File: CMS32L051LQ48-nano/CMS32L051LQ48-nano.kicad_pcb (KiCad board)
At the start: 4 copper layers, 18 x 43.2 mm, 26 parts, among them J101 Board Pin, J102 Board Pin, J103 USB_B_Micro, J105 Connection to DAPLink Board, U201 CMS32L051LQ48, U301 AP2127K-ADJ

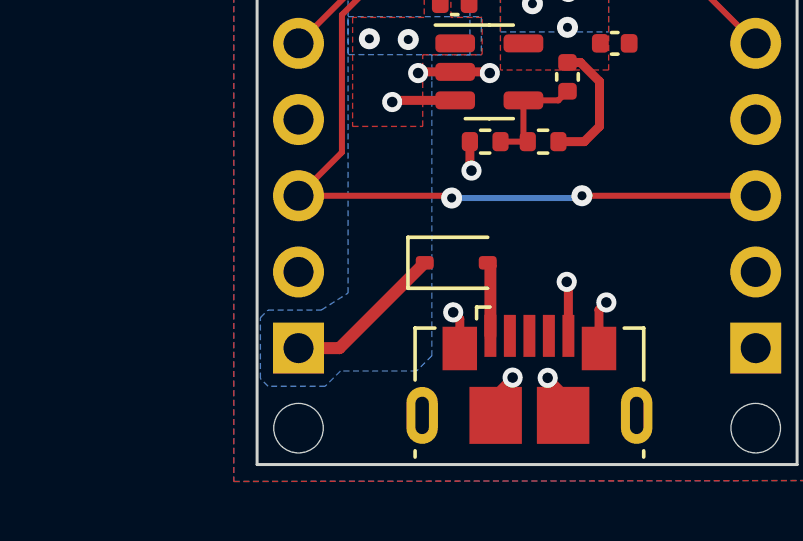
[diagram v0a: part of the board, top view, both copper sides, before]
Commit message: L051: added Vin zone
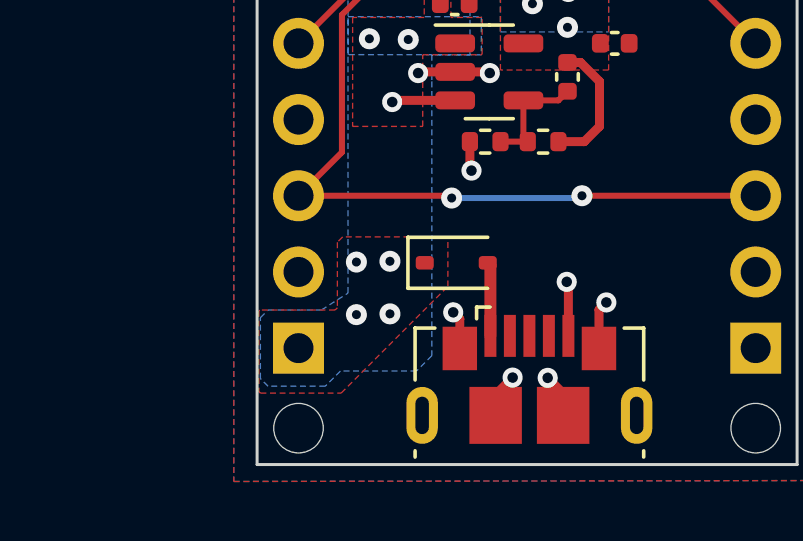
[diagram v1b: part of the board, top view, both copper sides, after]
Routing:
- net /V_{IN}: track 7.51 -> 2.12 mm, vias 3 -> 7
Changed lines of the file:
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@@
   (via (at 99.5934 72.1868) (size 0.67) (drill 0.35) (layers "F.Cu" "B.Cu") (net 2))
   (via (at 100.6348 85.8012) (size 0.67) (drill 0.35) (layers "F.Cu" "B.Cu") (net 2))
-  (segment (start 93.057 88.011) (end 91.694 88.011) (width 0.4) (layer "F.Cu") (net 3))
   (segment (start 94.873 79.752) (end 94.8182 79.8068) (width 0.3) (layer "F.Cu") (net 3))
   (segment (start 96.916 79.752) (end 94.873 79.752) (width 0.3) (layer "F.Cu") (net 3))
-  (segment (start 95.9018 85.1662) (end 93.057 88.011) (width 0.4) (layer "F.Cu") (net 3))
   (via (at 94.0562 77.6986) (size 0.7) (drill 0.3) (layers "F.Cu" "B.Cu") (free) (net 3))
+  (via (at 94.742 86.868) (size 0.7) (drill 0.3) (layers "F.Cu" "B.Cu") (free) (net 3))
+  (via (at 93.6244 85.1408) (size 0.7) (drill 0.3) (layers "F.Cu" "B.Cu") (free) (net 3))
+  (via (at 93.6244 86.8934) (size 0.7) (drill 0.3) (layers "F.Cu" "B.Cu") (free) (net 3))
   (via (at 94.8182 79.8068) (size 0.67) (drill 0.35) (layers "F.Cu" "B.Cu") (net 3))
   (via (at 95.3516 77.724) (size 0.7) (drill 0.3) (layers "F.Cu" "B.Cu") (free) (net 3))
+  (via (at 94.742 85.1154) (size 0.7) (drill 0.3) (layers "F.Cu" "B.Cu") (free) (net 3))
   (segment (start 99.191 79.752) (end 99.191 80.9812) (width 0.2) (layer "F.Cu") (net 4))
   (segment (start 99.191 80.9812) (end 99.3374 81.1276) (width 0.2) (layer "F.Cu") (net 4))
@@
   (segment (start 95.885 56.880929) (end 95.885 50.3428) (width 0.2) (layer "F.Cu") (net 59))
   (segment (start 97.0386 58.034529) (end 95.885 56.880929) (width 0.2) (layer "F.Cu") (net 59))
+  (zone (net 3) (net_name "/V_{IN}") (layer "F.Cu") (name "V_in") (hatch edge 0.5)
+    (priority 25)
+    (connect_pads yes (clearance 0.15))
+    (min_thickness 0.1) (filled_areas_thickness no)
+    (fill yes (thermal_gap 0.1) (thermal_bridge_width 0.2))
+    (polygon
+      (pts
+        (xy 96.6724 84.3026)
+        (xy 93.1672 84.3026)
+        (xy 92.9894 84.4804)
+        (xy 92.9894 86.6648)
+        (xy 92.9132 86.741)
+        (xy 90.3986 86.741)
+        (xy 90.3732 86.7664)
+        (xy 90.3732 89.4588)
+        (xy 90.424 89.5096)
+        (xy 93.1164 89.5096)
+        (xy 96.6724 85.9536)
+      )
+    )
+  )
   (zone (net 5) (net_name "/Regulator_V_{OUT}") (layer "F.Cu") (name "RegV_{OUT}") (hatch edge 0.5)
     (priority 20)

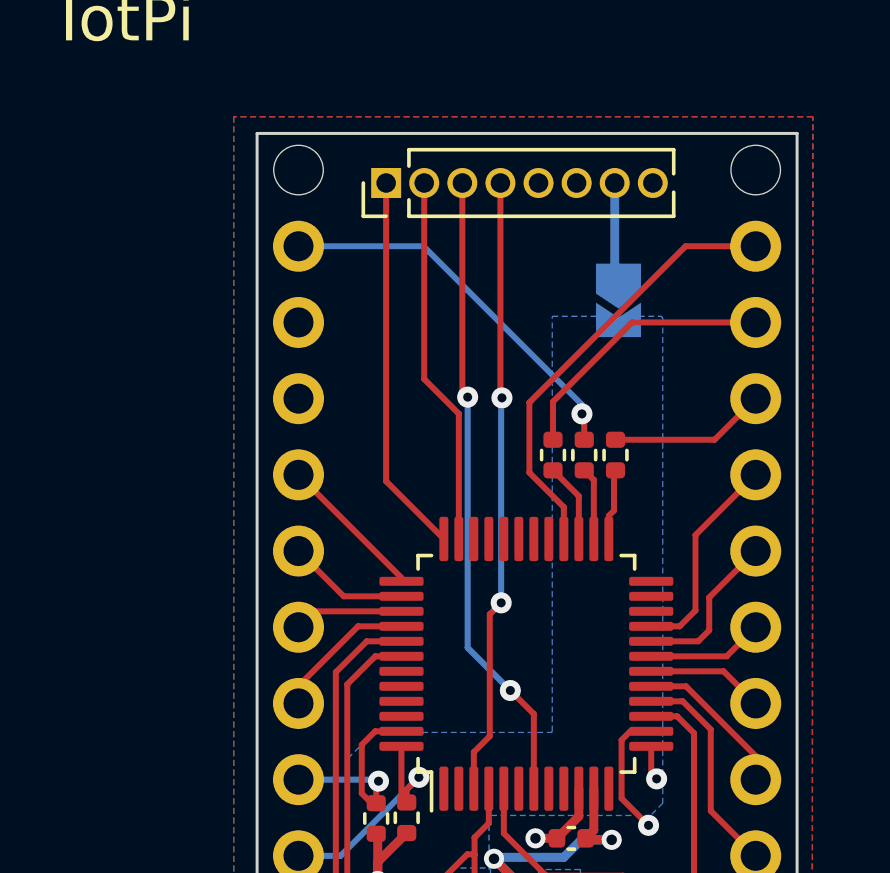
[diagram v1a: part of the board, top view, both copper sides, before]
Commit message: L051: make space for LEDs
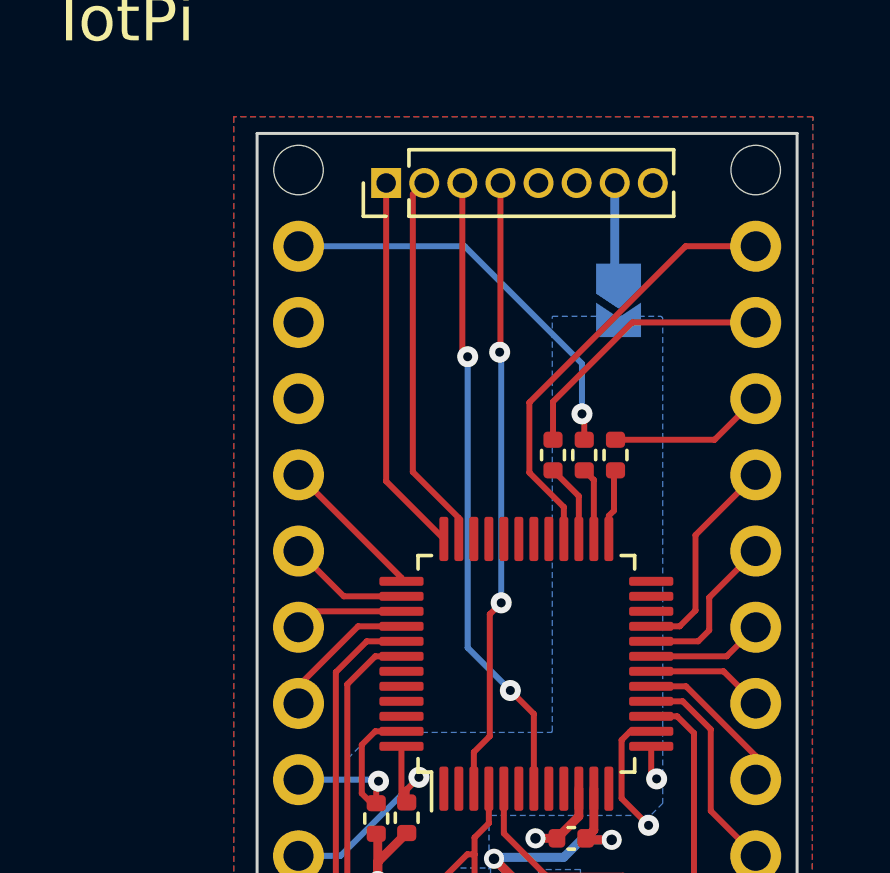
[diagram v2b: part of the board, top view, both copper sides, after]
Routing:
- net /MCU/D13/SCK: track 12.8 -> 13.6 mm
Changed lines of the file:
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@@
   (via (at 99.4918 76.5302) (size 0.7) (drill 0.3) (layers "F.Cu" "B.Cu") (free) (net 5))
   (via (at 100.6602 77.3176) (size 0.7) (drill 0.3) (layers "F.Cu" "B.Cu") (free) (net 5))
-  (segment (start 97.155 57.3024) (end 97.155 50.3428) (width 0.2) (layer "F.Cu") (net 6))
+  (segment (start 97.3328 56.134) (end 97.155 55.9562) (width 0.2) (layer "F.Cu") (net 6))
+  (segment (start 97.155 55.9562) (end 97.155 50.3428) (width 0.2) (layer "F.Cu") (net 6))
   (segment (start 98.7552 67.2592) (end 99.5386 68.0426) (width 0.2) (layer "F.Cu") (net 6))
-  (segment (start 97.3328 57.4802) (end 97.155 57.3024) (width 0.2) (layer "F.Cu") (net 6))
   (segment (start 99.5386 68.0426) (end 99.5386 70.5327) (width 0.2) (layer "F.Cu") (net 6))
-  (via (at 97.3328 57.4802) (size 0.7) (drill 0.3) (layers "F.Cu" "B.Cu") (net 6))
+  (via (at 97.3328 56.134) (size 0.7) (drill 0.3) (layers "F.Cu" "B.Cu") (net 6))
   (via (at 98.7552 67.2592) (size 0.7) (drill 0.3) (layers "F.Cu" "B.Cu") (net 6))
-  (segment (start 97.3328 65.8368) (end 97.3328 57.4802) (width 0.2) (layer "B.Cu") (net 6))
-  (segment (start 98.7552 67.2592) (end 97.3328 65.8368) (width 0.2) (layer "B.Cu") (net 6))
+  (segment (start 97.3328 56.134) (end 97.3328 65.8368) (width 0.2) (layer "B.Cu") (net 6))
+  (segment (start 97.3328 65.8368) (end 98.7552 67.2592) (width 0.2) (layer "B.Cu") (net 6))
+  (segment (start 98.425 55.9562) (end 98.425 50.3428) (width 0.2) (layer "F.Cu") (net 7))
   (segment (start 97.5386 70.5327) (end 97.5386 69.314) (width 0.2) (layer "F.Cu") (net 7))
   (segment (start 97.5386 69.314) (end 98.0694 68.7832) (width 0.2) (layer "F.Cu") (net 7))
   (segment (start 98.0694 64.7192) (end 98.4504 64.3382) (width 0.2) (layer "F.Cu") (net 7))
-  (segment (start 98.4758 57.5056) (end 98.425 57.4548) (width 0.2) (layer "F.Cu") (net 7))
   (segment (start 98.0694 68.7832) (end 98.0694 64.7192) (width 0.2) (layer "F.Cu") (net 7))
-  (segment (start 98.425 57.4548) (end 98.425 50.3428) (width 0.2) (layer "F.Cu") (net 7))
+  (segment (start 98.3996 55.9816) (end 98.425 55.9562) (width 0.2) (layer "F.Cu") (net 7))
   (via (at 98.4504 64.3382) (size 0.7) (drill 0.3) (layers "F.Cu" "B.Cu") (net 7))
-  (via (at 98.4758 57.5056) (size 0.7) (drill 0.3) (layers "F.Cu" "B.Cu") (net 7))
-  (segment (start 98.4504 57.531) (end 98.4758 57.5056) (width 0.2) (layer "B.Cu") (net 7))
-  (segment (start 98.4504 64.3382) (end 98.4504 57.531) (width 0.2) (layer "B.Cu") (net 7))
+  (via (at 98.3996 55.9816) (size 0.7) (drill 0.3) (layers "F.Cu" "B.Cu") (net 7))
+  (segment (start 98.4504 56.0324) (end 98.4504 64.3382) (width 0.2) (layer "B.Cu") (net 7))
+  (segment (start 98.3996 55.9816) (end 98.4504 56.0324) (width 0.2) (layer "B.Cu") (net 7))
   (segment (start 97.6604 75.1586) (end 97.6604 74.1686) (width 0.2) (layer "F.Cu") (net 15))
   (segment (start 98.0386 71.6842) (end 98.0386 70.5327) (width 0.2) (layer "F.Cu") (net 15))
@@
   (segment (start 101.219 58.9006) (end 101.219 58.1152) (width 0.2) (layer "F.Cu") (net 37))
   (via (at 101.1428 58.039) (size 0.7) (drill 0.3) (layers "F.Cu" "B.Cu") (net 37))
-  (segment (start 101.1428 58.039) (end 101.1428 57.7342) (width 0.2) (layer "B.Cu") (net 37))
-  (segment (start 95.8596 52.451) (end 91.694 52.451) (width 0.2) (layer "B.Cu") (net 37))
-  (segment (start 101.1428 57.7342) (end 95.8596 52.451) (width 0.2) (layer "B.Cu") (net 37))
+  (segment (start 101.1428 58.039) (end 101.1428 56.3626) (width 0.2) (layer "B.Cu") (net 37))
+  (segment (start 97.2312 52.451) (end 91.694 52.451) (width 0.2) (layer "B.Cu") (net 37))
+  (segment (start 101.1428 56.3626) (end 97.2312 52.451) (width 0.2) (layer "B.Cu") (net 37))
   (segment (start 101.5386 62.2077) (end 101.5386 60.2402) (width 0.2) (layer "F.Cu") (net 38))
   (segment (start 101.5386 60.2402) (end 101.219 59.9206) (width 0.2) (layer "F.Cu") (net 38))
@@
   (segment (start 96.5386 62.2077) (end 94.615 60.2841) (width 0.2) (layer "F.Cu") (net 58))
   (segment (start 94.615 60.2841) (end 94.615 50.3428) (width 0.2) (layer "F.Cu") (net 58))
-  (segment (start 97.0386 62.2077) (end 97.0386 58.034529) (width 0.2) (layer "F.Cu") (net 59))
-  (segment (start 95.885 56.880929) (end 95.885 50.3428) (width 0.2) (layer "F.Cu") (net 59))
-  (segment (start 97.0386 58.034529) (end 95.885 56.880929) (width 0.2) (layer "F.Cu") (net 59))
+  (segment (start 95.504 59.975981) (end 95.504 50.7238) (width 0.2) (layer "F.Cu") (net 59))
+  (segment (start 97.0386 62.2077) (end 97.0386 61.510581) (width 0.2) (layer "F.Cu") (net 59))
+  (segment (start 97.0386 61.510581) (end 95.504 59.975981) (width 0.2) (layer "F.Cu") (net 59))
+  (segment (start 95.504 50.7238) (end 95.885 50.3428) (width 0.2) (layer "F.Cu") (net 59))
   (zone (net 3) (net_name "/V_{IN}") (layer "F.Cu") (name "V_in") (hatch edge 0.5)
     (priority 25)

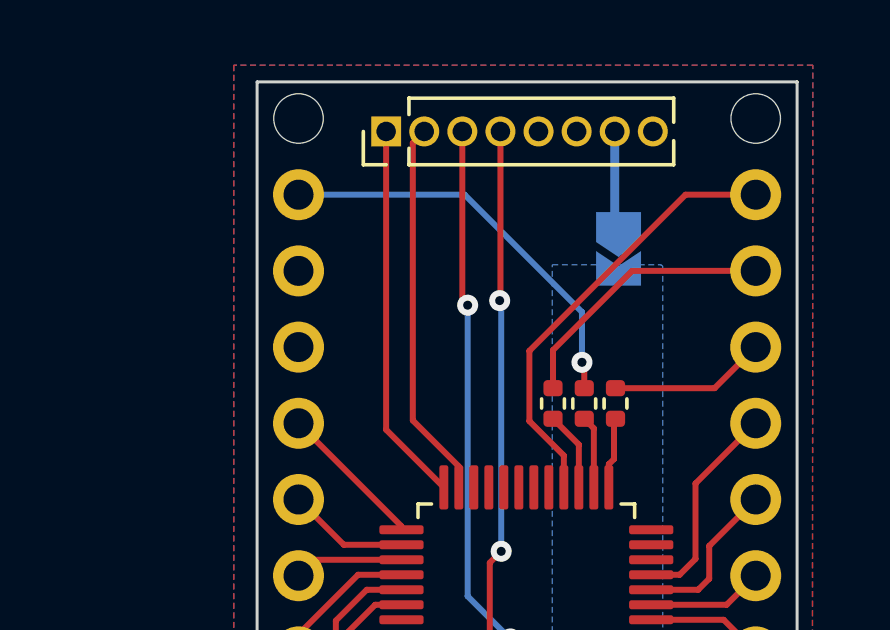
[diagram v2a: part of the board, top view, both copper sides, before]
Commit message: added two LEDs
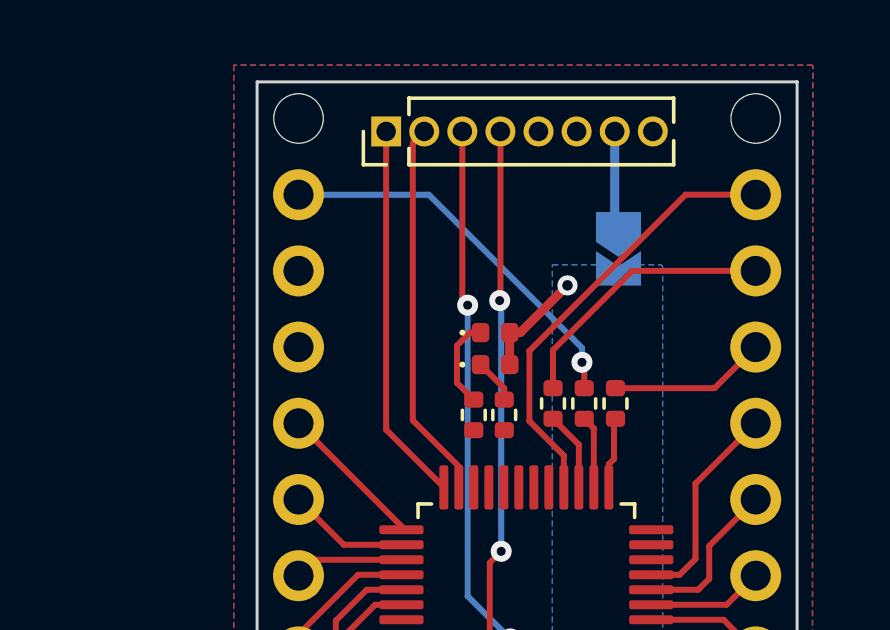
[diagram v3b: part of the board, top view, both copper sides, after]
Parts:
- added D201: LED, LED_SMD:LED_0402_1005Metric, F.Cu at (98.2, 57.0)
- added D202: LED, LED_SMD:LED_0402_1005Metric, F.Cu at (98.2, 58.1)
- added R207: 200R, Resistor_SMD:R_0402_1005Metric, F.Cu at (97.5, 59.8)
- added R208: 200R, Resistor_SMD:R_0402_1005Metric, F.Cu at (98.6, 59.8)
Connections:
- U201 pad 33: unconnected-(U201-P11-Pad33) -> /MCU/LED2
- U201 pad 34: unconnected-(U201-P10-Pad34) -> /MCU/LED1
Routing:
- net /V_{IN}: track 2.12 -> 5.77 mm, vias 7 -> 8
- net Net-(D201-K): track 0.00 -> 3.00 mm
- net Net-(D202-K): track 0.00 -> 1.49 mm
- net /MCU/D13/SCK: track 13.6 -> 12.9 mm

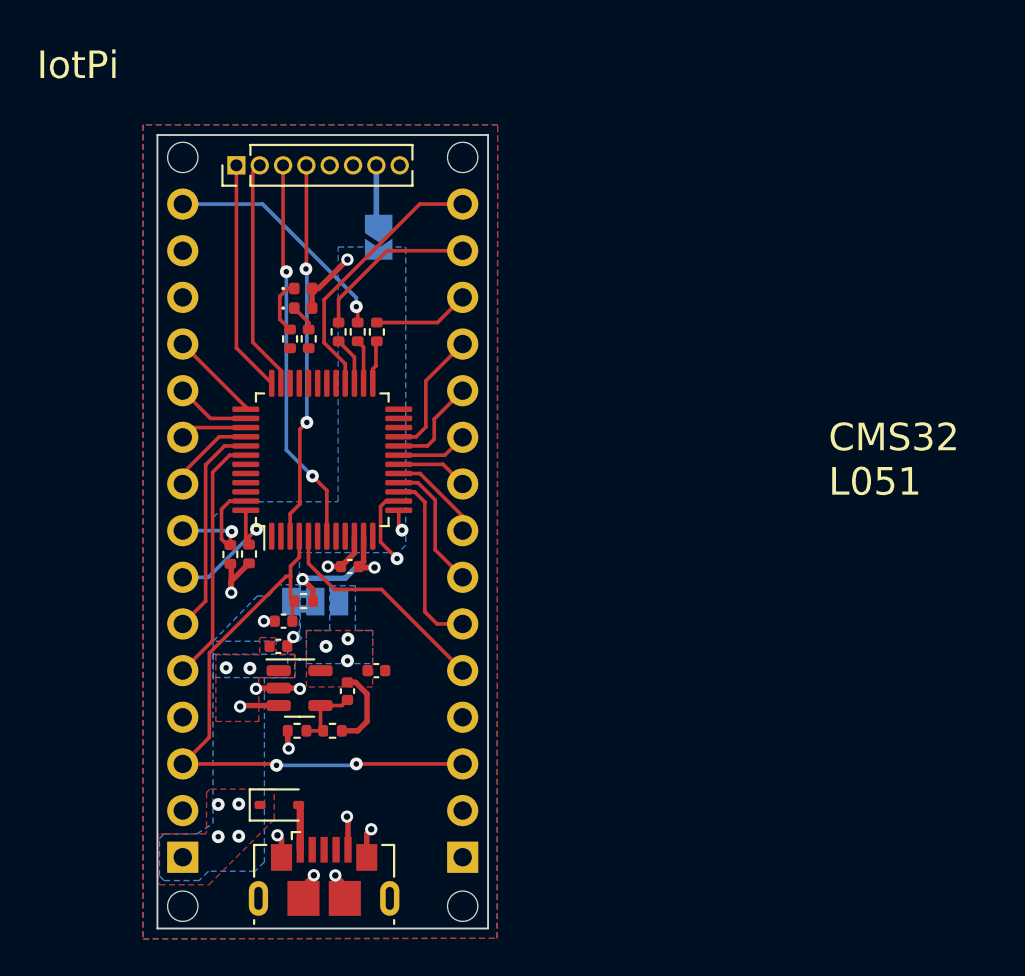
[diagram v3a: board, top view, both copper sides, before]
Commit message: added lables and KiCad logo
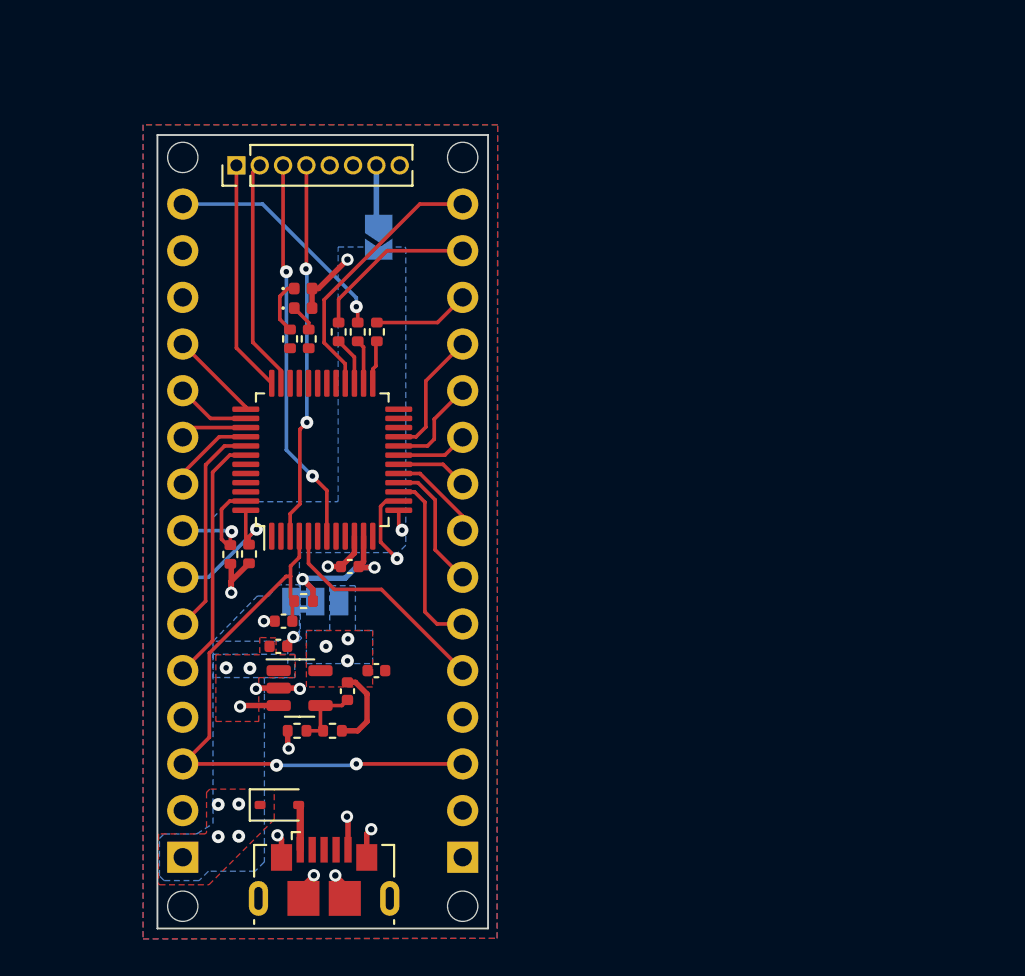
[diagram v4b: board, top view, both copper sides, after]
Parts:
- added REF**: KiCad-Logo2_5mm_SilkScreen, Symbol:KiCad-Logo2_5mm_SilkScreen, B.Cu at (98.9, 65.2)
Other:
- board text added: "A0"
- board text added: "A1"
- board text added: "A2"
- board text added: "A3"
- board text added: "A4"
- board text added: "A5"
- board text added: "A6"
- board text added: "A7"
- board text added: "D0"
- board text added: "D10"
- board text added: "D11"
- board text added: "D12"
- board text added: "D13"
- board text added: "D2"
- board text added: "D3"
- board text added: "D4"
- board text added: "D5"
- board text added: "D6"
- board text added: "D7"
- board text added: "D8"
- board text added: "D9"
- board text added: "MCU_V_{IN}"
- board text added: "~{RESET}"
- board text removed: "CMS32 L051"
- board text removed: "IotPi"
